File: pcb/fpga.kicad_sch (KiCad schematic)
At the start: 45 parts, among them U1 XC7A50T-FTG256, U2 410-251-B, U3 S70KL1283DPBHV020, U4 W25Q128JVS, Y1 ASE-20MHz

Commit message: layout prep
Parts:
- C1, C10, C11, C12, C13, C14, C15, C16, C17, C18, C19, C2, C20, C21, C22, C23, C24, C25, C26, C27, C28, C29, C3, C30, C4, C5, C6, C7, C8, C9: footprint (none) -> Capacitor_SMD:C_0805_2012Metric_Pad1.18x1.45mm_HandSolder
- R1, R10, R2, R3, R4, R5, R6, R7, R8, R9: footprint (none) -> Resistor_SMD:R_0805_2012Metric_Pad1.20x1.40mm_HandSolder
- U2: footprint IC11_410-251-B_DGT -> footprints:IC11_410-251-B_DGT
- U3: footprint (none) -> S70KL1283DPBHV020:BGA24C100P5X5_600X800X100
- Y1: footprint Oscillator:Oscillator_DIP-14 -> Oscillator:Oscillator_SMD_Abracon_ASV-4Pin_7.0x5.1mm_HandSoldering
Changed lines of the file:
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@@
 			)
 		)
-		(property "Footprint" ""
+		(property "Footprint" "Capacitor_SMD:C_0805_2012Metric_Pad1.18x1.45mm_HandSolder"
 			(at 360.3752 229.87 0)
 			(hide yes)
@@
 			)
 		)
-		(property "Footprint" ""
+		(property "Footprint" "Capacitor_SMD:C_0805_2012Metric_Pad1.18x1.45mm_HandSolder"
 			(at 276.5552 35.56 0)
 			(hide yes)
@@
 			)
 		)
-		(property "Footprint" ""
+		(property "Footprint" "Resistor_SMD:R_0805_2012Metric_Pad1.20x1.40mm_HandSolder"
 			(at 106.68 79.248 90)
 			(hide yes)
@@
 			)
 		)
-		(property "Footprint" ""
+		(property "Footprint" "Capacitor_SMD:C_0805_2012Metric_Pad1.18x1.45mm_HandSolder"
 			(at 261.3152 35.56 0)
 			(hide yes)
@@
 			)
 		)
-		(property "Footprint" ""
+		(property "Footprint" "Capacitor_SMD:C_0805_2012Metric_Pad1.18x1.45mm_HandSolder"
 			(at 284.1752 35.56 0)
 			(hide yes)
@@
 			)
 		)
-		(property "Footprint" ""
+		(property "Footprint" "Capacitor_SMD:C_0805_2012Metric_Pad1.18x1.45mm_HandSolder"
 			(at 307.0352 35.56 0)
 			(hide yes)
@@
 			)
 		)
-		(property "Footprint" ""
+		(property "Footprint" "Resistor_SMD:R_0805_2012Metric_Pad1.20x1.40mm_HandSolder"
 			(at 164.592 62.23 90)
 			(hide yes)
@@
 			)
 		)
-		(property "Footprint" ""
+		(property "Footprint" "Capacitor_SMD:C_0805_2012Metric_Pad1.18x1.45mm_HandSolder"
 			(at 268.9352 35.56 0)
 			(hide yes)
@@
 			)
 		)
-		(property "Footprint" ""
+		(property "Footprint" "Resistor_SMD:R_0805_2012Metric_Pad1.20x1.40mm_HandSolder"
 			(at 119.38 57.658 90)
 			(hide yes)
@@
 			)
 		)
-		(property "Footprint" ""
+		(property "Footprint" "Capacitor_SMD:C_0805_2012Metric_Pad1.18x1.45mm_HandSolder"
 			(at 164.7952 226.06 0)
 			(hide yes)
@@
 			)
 		)
-		(property "Footprint" ""
+		(property "Footprint" "Capacitor_SMD:C_0805_2012Metric_Pad1.18x1.45mm_HandSolder"
 			(at 176.2252 49.53 0)
 			(hide yes)
@@
 			)
 		)
-		(property "Footprint" ""
+		(property "Footprint" "Capacitor_SMD:C_0805_2012Metric_Pad1.18x1.45mm_HandSolder"
 			(at 296.8752 229.87 0)
 			(hide yes)
@@
 			)
 		)
-		(property "Footprint" ""
+		(property "Footprint" "Capacitor_SMD:C_0805_2012Metric_Pad1.18x1.45mm_HandSolder"
 			(at 157.1752 226.06 0)
 			(hide yes)
@@
 			)
 		)
-		(property "Footprint" ""
+		(property "Footprint" "Capacitor_SMD:C_0805_2012Metric_Pad1.18x1.45mm_HandSolder"
 			(at 289.2552 229.87 0)
 			(hide yes)
@@
 			)
 		)
-		(property "Footprint" ""
+		(property "Footprint" "Capacitor_SMD:C_0805_2012Metric_Pad1.18x1.45mm_HandSolder"
 			(at 352.7552 229.87 0)
 			(hide yes)
@@
 			)
 		)
-		(property "Footprint" ""
+		(property "Footprint" "Capacitor_SMD:C_0805_2012Metric_Pad1.18x1.45mm_HandSolder"
 			(at 354.0252 35.56 0)
 			(hide yes)
@@
 			)
 		)
-		(property "Footprint" ""
+		(property "Footprint" "Resistor_SMD:R_0805_2012Metric_Pad1.20x1.40mm_HandSolder"
 			(at 173.482 62.23 90)
 			(hide yes)
@@
 			)
 		)
-		(property "Footprint" ""
+		(property "Footprint" "Capacitor_SMD:C_0805_2012Metric_Pad1.18x1.45mm_HandSolder"
 			(at 312.1152 229.87 0)
 			(hide yes)
@@
 			)
 		)
-		(property "Footprint" ""
+		(property "Footprint" "Capacitor_SMD:C_0805_2012Metric_Pad1.18x1.45mm_HandSolder"
 			(at 346.4052 35.56 0)
 			(hide yes)
@@
 			)
 		)
-		(property "Footprint" ""
+		(property "Footprint" "Capacitor_SMD:C_0805_2012Metric_Pad1.18x1.45mm_HandSolder"
 			(at 314.6552 35.56 0)
 			(hide yes)
@@
 			)
 		)
-		(property "Footprint" ""
+		(property "Footprint" "Capacitor_SMD:C_0805_2012Metric_Pad1.18x1.45mm_HandSolder"
 			(at 383.2352 229.87 0)
 			(hide yes)
@@
 			)
 		)
-		(property "Footprint" ""
+		(property "Footprint" "Capacitor_SMD:C_0805_2012Metric_Pad1.18x1.45mm_HandSolder"
 			(at 345.1352 229.87 0)
 			(hide yes)
@@
 			)
 		)
-		(property "Footprint" ""
+		(property "Footprint" "Capacitor_SMD:C_0805_2012Metric_Pad1.18x1.45mm_HandSolder"
 			(at 230.1748 121.92 0)
 			(hide yes)
@@
 			)
 		)
-		(property "Footprint" ""
+		(property "Footprint" "Resistor_SMD:R_0805_2012Metric_Pad1.20x1.40mm_HandSolder"
 			(at 119.38 62.738 90)
 			(hide yes)
@@
 			)
 		)
-		(property "Footprint" ""
+		(property "Footprint" "Resistor_SMD:R_0805_2012Metric_Pad1.20x1.40mm_HandSolder"
 			(at 119.38 52.578 90)
 			(hide yes)
@@
 			)
 		)
-		(property "Footprint" ""
+		(property "Footprint" "Capacitor_SMD:C_0805_2012Metric_Pad1.18x1.45mm_HandSolder"
 			(at 367.9952 229.87 0)
 			(hide yes)
@@
 			)
 		)
-		(property "Footprint" ""
+		(property "Footprint" "Capacitor_SMD:C_0805_2012Metric_Pad1.18x1.45mm_HandSolder"
 			(at 323.5452 35.56 0)
 			(hide yes)
@@
 			)
 		)
-		(property "Footprint" ""
+		(property "Footprint" "Resistor_SMD:R_0805_2012Metric_Pad1.20x1.40mm_HandSolder"
 			(at 106.68 84.328 90)
 			(hide yes)
@@
 			)
 		)
-		(property "Footprint" ""
+		(property "Footprint" "Capacitor_SMD:C_0805_2012Metric_Pad1.18x1.45mm_HandSolder"
 			(at 299.4152 35.56 0)
 			(hide yes)
@@
 			)
 		)
-		(property "Footprint" ""
+		(property "Footprint" "Resistor_SMD:R_0805_2012Metric_Pad1.20x1.40mm_HandSolder"
 			(at 106.68 89.408 90)
 			(hide yes)
@@
 			)
 		)
-		(property "Footprint" ""
+		(property "Footprint" "Resistor_SMD:R_0805_2012Metric_Pad1.20x1.40mm_HandSolder"
 			(at 155.702 62.23 90)
 			(hide yes)
@@
 			)
 		)
-		(property "Footprint" ""
+		(property "Footprint" "Capacitor_SMD:C_0805_2012Metric_Pad1.18x1.45mm_HandSolder"
 			(at 291.7952 35.56 0)
 			(hide yes)
@@
 			)
 		)
-		(property "Footprint" ""
+		(property "Footprint" "Resistor_SMD:R_0805_2012Metric_Pad1.20x1.40mm_HandSolder"
 			(at 106.68 94.488 90)
 			(hide yes)
@@
 			)
 		)
-		(property "Footprint" ""
+		(property "Footprint" "Capacitor_SMD:C_0805_2012Metric_Pad1.18x1.45mm_HandSolder"
 			(at 304.4952 229.87 0)
 			(hide yes)
@@
 			)
 		)
-		(property "Footprint" ""
+		(property "Footprint" "Capacitor_SMD:C_0805_2012Metric_Pad1.18x1.45mm_HandSolder"
 			(at 280.67 226.06 0)
 			(hide yes)
@@
 			)
 		)
-		(property "Footprint" ""
+		(property "Footprint" "Capacitor_SMD:C_0805_2012Metric_Pad1.18x1.45mm_HandSolder"
 			(at 361.6452 35.56 0)
 			(hide yes)
@@
 			)
 		)
-		(property "Footprint" ""
+		(property "Footprint" "Capacitor_SMD:C_0805_2012Metric_Pad1.18x1.45mm_HandSolder"
 			(at 369.2652 35.56 0)
 			(hide yes)
@@
 			)
 		)
-		(property "Footprint" ""
+		(property "Footprint" "S70KL1283DPBHV020:BGA24C100P5X5_600X800X100"
 			(at 152.4 88.9 0)
 			(hide yes)
@@
 			)
 		)
-		(property "Footprint" ""
+		(property "Footprint" "Capacitor_SMD:C_0805_2012Metric_Pad1.18x1.45mm_HandSolder"
 			(at 331.1652 35.56 0)
 			(hide yes)
@@
 			)
 		)
-		(property "Footprint" ""
+		(property "Footprint" "Capacitor_SMD:C_0805_2012Metric_Pad1.18x1.45mm_HandSolder"
 			(at 375.6152 229.87 0)
 			(hide yes)
@@
 			)
 		)
-		(property "Footprint" ""
+		(property "Footprint" "Capacitor_SMD:C_0805_2012Metric_Pad1.18x1.45mm_HandSolder"
 			(at 338.7852 35.56 0)
 			(hide yes)
@@
 			)
 		)
-		(property "Footprint" "IC11_410-251-B_DGT"
+		(property "Footprint" "footprints:IC11_410-251-B_DGT"
 			(at 119.38 25.4 0)
 			(hide yes)
@@
 			)
 		)
-		(property "Footprint" "Oscillator:Oscillator_DIP-14"
+		(property "Footprint" "Oscillator:Oscillator_SMD_Abracon_ASV-4Pin_7.0x5.1mm_HandSoldering"
 			(at 259.08 124.46 0)
 			(hide yes)

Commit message: pcb/fpga: fix vga
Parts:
- added J?: DE15_Socket_HighDensity, Connector_Dsub:DSUB-15_Socket_EdgeMount_P2.77mm, symbol Connector:DE15_Socket_HighDensity
- added R? (x3): 510, symbol Device:R
- added R? (x3): 2.0k, symbol Device:R
- added R? (x3): 1.0k, symbol Device:R
- added R? (x2): 100, symbol Device:R
- added R? (x3): 3.9k, symbol Device:R
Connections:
- net +3V3: now also U1.M3 (VCCO_34), U1.R4 (VCCO_34), U1.T1 (VCCO_34)
- net GND: now also J?.10, J?.5, J?.6, J?.7, J?.8; no longer U1.M3 (VCCO_34), U1.R4 (VCCO_34), U1.T1 (VCCO_34)
- net at U1.M5 (IO_L6P_T0_34): now also R?.2
- net at U1.N1 (IO_L4P_T0_34): now also R?.2
- net at U1.N2 (IO_L3N_T0_DQS_34): now also R?.2
- net at U1.N4 (IO_L6N_T0_VREF_34): now also R?.2
- net at U1.P1 (IO_L4N_T0_34): now also R?.2
- net at U1.P3 (IO_L5N_T0_34): now also R?.2
- net at U1.P4 (IO_L5P_T0_34): now also R?.2
- net at U1.P5 (IO_L10P_T1_34): now also R?.2
- net at U1.R1 (IO_L7N_T1_34): now also R?.2
- net at U1.R2 (IO_L7P_T1_34): now also R?.2
- net at U1.R3 (IO_L8P_T1_34): now also R?.2
- net at U1.T2 (IO_L8N_T1_34): now also R?.2
- net at U1.T3 (IO_L9N_T1_DQS_34): now also R?.2
- net at U1.T4 (IO_L9P_T1_DQS_34): now also R?.2
- new net BLUE_ANALOG: J?.3, R?.1, R?.1, R?.1, R?.1
- new net GREEN_ANALOG: J?.2, R?.1, R?.1, R?.1, R?.1
- new net HSYNC: J?.13, R?.1
- new net RED_ANALOG: J?.1, R?.1, R?.1, R?.1, R?.1
- new net VSYNC: J?.14, R?.1
- no-connect marks 138 -> 129
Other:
- moved on the sheet: C1, C10, C12, C14, C16, C2, C21, C23, C25, C27, C29, C30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

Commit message: updates labels
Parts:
- gave numbers to parts that had none: 15
- renumbered C3 to C1, C17 to C10, C18 to C11, C1 to C12, C19 to C13, C2 to C14, C20 to C15, C22 to C16, C24 to C17, C21 to C18, C8 to C19, C4 to C2, C26 to C20, C23 to C21, C10 to C22, C28 to C23, C25 to C24, C12 to C25, C27 to C26, C14 to C27, C29 to C28, C16 to C29, C5 to C3, C6 to C4, C7 to C5, C9 to C6, C11 to C7, C13 to C8, C15 to C9, R8 to R22, R9 to R23, R10 to R24

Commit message: started layout
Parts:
- R10, R11, R12, R13, R14, R15, R16, R17, R18, R19, R20, R21, R8, R9: footprint (none) -> Resistor_SMD:R_0805_2012Metric_Pad1.20x1.40mm_HandSolder
- U2: footprint footprints:IC11_410-251-B_DGT -> 410_251_B:IC11_410-251-B_DGT
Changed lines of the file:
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@@
 			)
 		)
-		(property "Footprint" ""
+		(property "Footprint" "Resistor_SMD:R_0805_2012Metric_Pad1.20x1.40mm_HandSolder"
 			(at 129.54 221.742 90)
 			(hide yes)
@@
 			)
 		)
-		(property "Footprint" ""
+		(property "Footprint" "Resistor_SMD:R_0805_2012Metric_Pad1.20x1.40mm_HandSolder"
 			(at 129.54 216.662 90)
 			(hide yes)
@@
 			)
 		)
-		(property "Footprint" ""
+		(property "Footprint" "Resistor_SMD:R_0805_2012Metric_Pad1.20x1.40mm_HandSolder"
 			(at 129.54 211.582 90)
 			(hide yes)
@@
 			)
 		)
-		(property "Footprint" ""
+		(property "Footprint" "Resistor_SMD:R_0805_2012Metric_Pad1.20x1.40mm_HandSolder"
 			(at 129.54 219.202 90)
 			(hide yes)
@@
 			)
 		)
-		(property "Footprint" ""
+		(property "Footprint" "Resistor_SMD:R_0805_2012Metric_Pad1.20x1.40mm_HandSolder"
 			(at 129.54 234.442 90)
 			(hide yes)
@@
 			)
 		)
-		(property "Footprint" ""
+		(property "Footprint" "Resistor_SMD:R_0805_2012Metric_Pad1.20x1.40mm_HandSolder"
 			(at 129.54 214.122 90)
 			(hide yes)
@@
 			)
 		)
-		(property "Footprint" ""
+		(property "Footprint" "Resistor_SMD:R_0805_2012Metric_Pad1.20x1.40mm_HandSolder"
 			(at 129.54 224.282 90)
 			(hide yes)
@@
 			)
 		)
-		(property "Footprint" ""
+		(property "Footprint" "Resistor_SMD:R_0805_2012Metric_Pad1.20x1.40mm_HandSolder"
 			(at 129.54 226.822 90)
 			(hide yes)
@@
 			)
 		)
-		(property "Footprint" ""
+		(property "Footprint" "Resistor_SMD:R_0805_2012Metric_Pad1.20x1.40mm_HandSolder"
 			(at 129.54 231.902 90)
 			(hide yes)
@@
 			)
 		)
-		(property "Footprint" ""
+		(property "Footprint" "Resistor_SMD:R_0805_2012Metric_Pad1.20x1.40mm_HandSolder"
 			(at 129.54 229.362 90)
 			(hide yes)
@@
 			)
 		)
-		(property "Footprint" ""
+		(property "Footprint" "Resistor_SMD:R_0805_2012Metric_Pad1.20x1.40mm_HandSolder"
 			(at 129.54 203.962 90)
 			(hide yes)
@@
 			)
 		)
-		(property "Footprint" ""
+		(property "Footprint" "Resistor_SMD:R_0805_2012Metric_Pad1.20x1.40mm_HandSolder"
 			(at 129.54 206.502 90)
 			(hide yes)
@@
 			)
 		)
-		(property "Footprint" ""
+		(property "Footprint" "Resistor_SMD:R_0805_2012Metric_Pad1.20x1.40mm_HandSolder"
 			(at 129.54 236.982 90)
 			(hide yes)
@@
 			)
 		)
-		(property "Footprint" "footprints:IC11_410-251-B_DGT"
+		(property "Footprint" "410_251_B:IC11_410-251-B_DGT"
 			(at 119.38 25.4 0)
 			(hide yes)
@@
 			)
 		)
-		(property "Footprint" ""
+		(property "Footprint" "Resistor_SMD:R_0805_2012Metric_Pad1.20x1.40mm_HandSolder"
 			(at 129.54 209.042 90)
 			(hide yes)

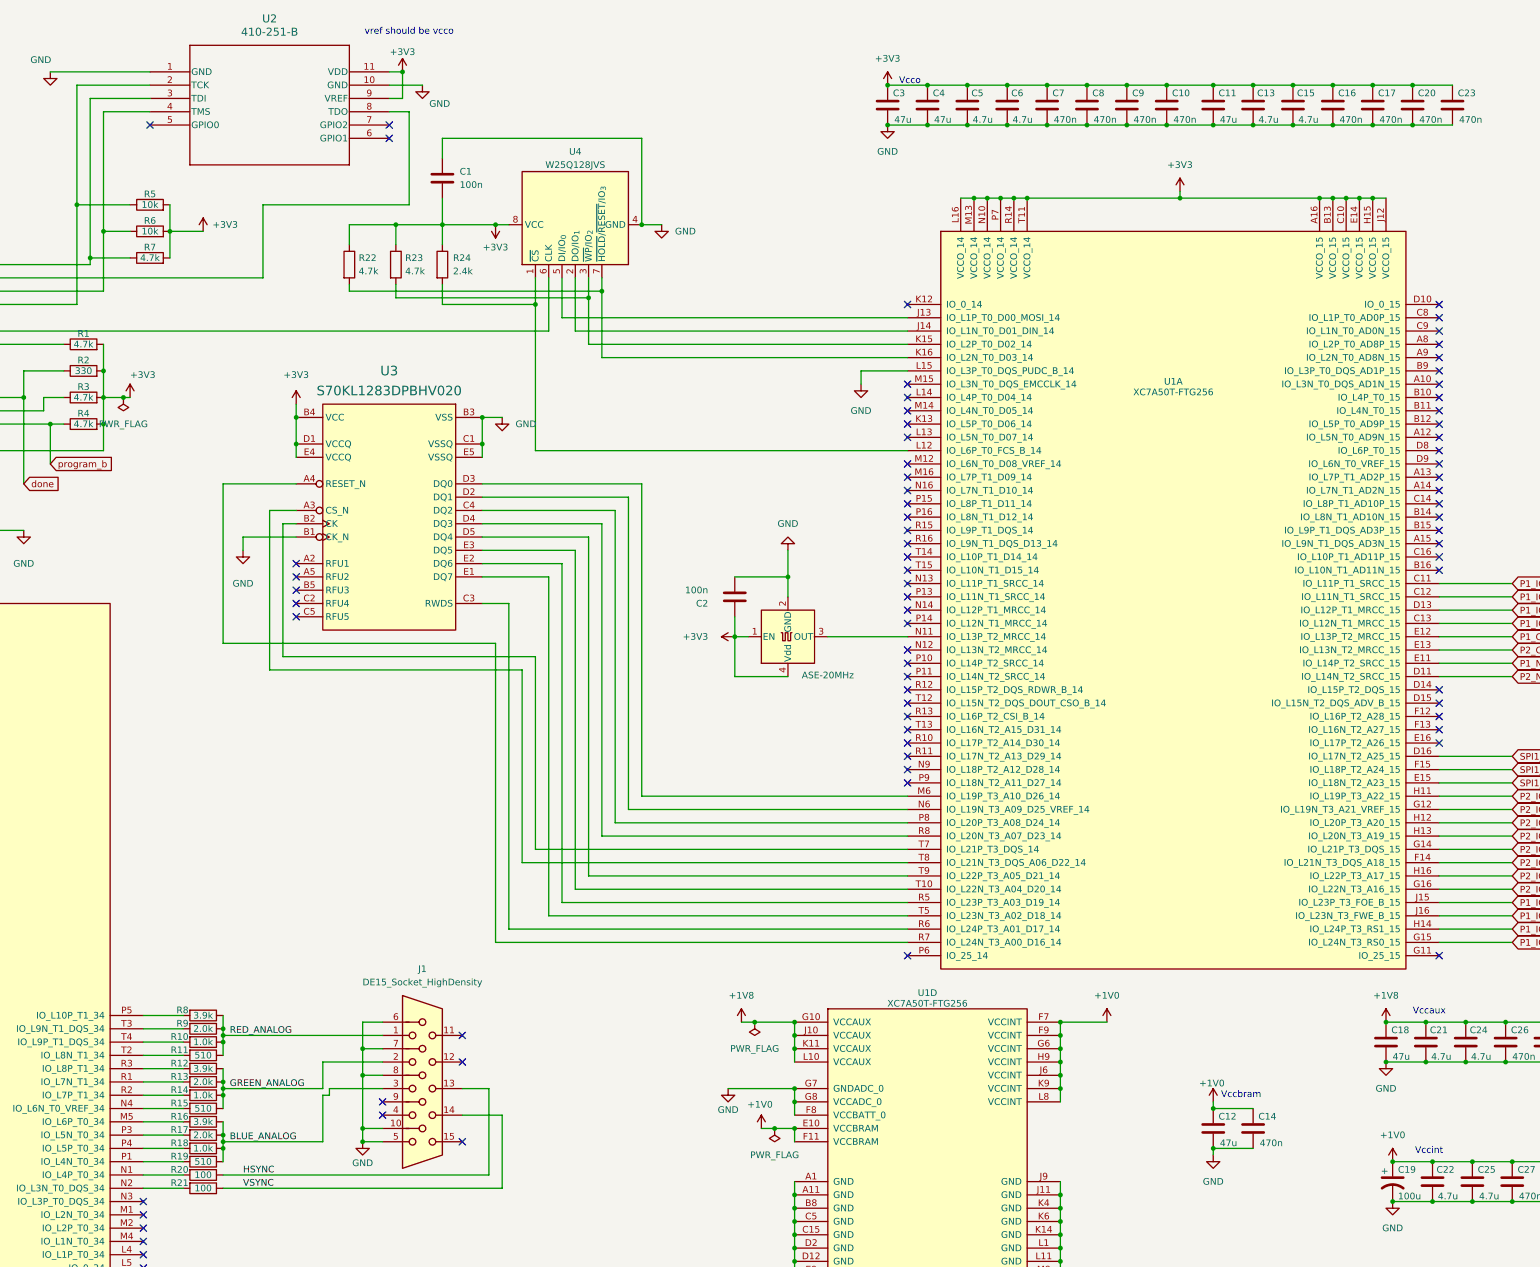
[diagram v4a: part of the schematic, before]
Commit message: pcb: finalize erc
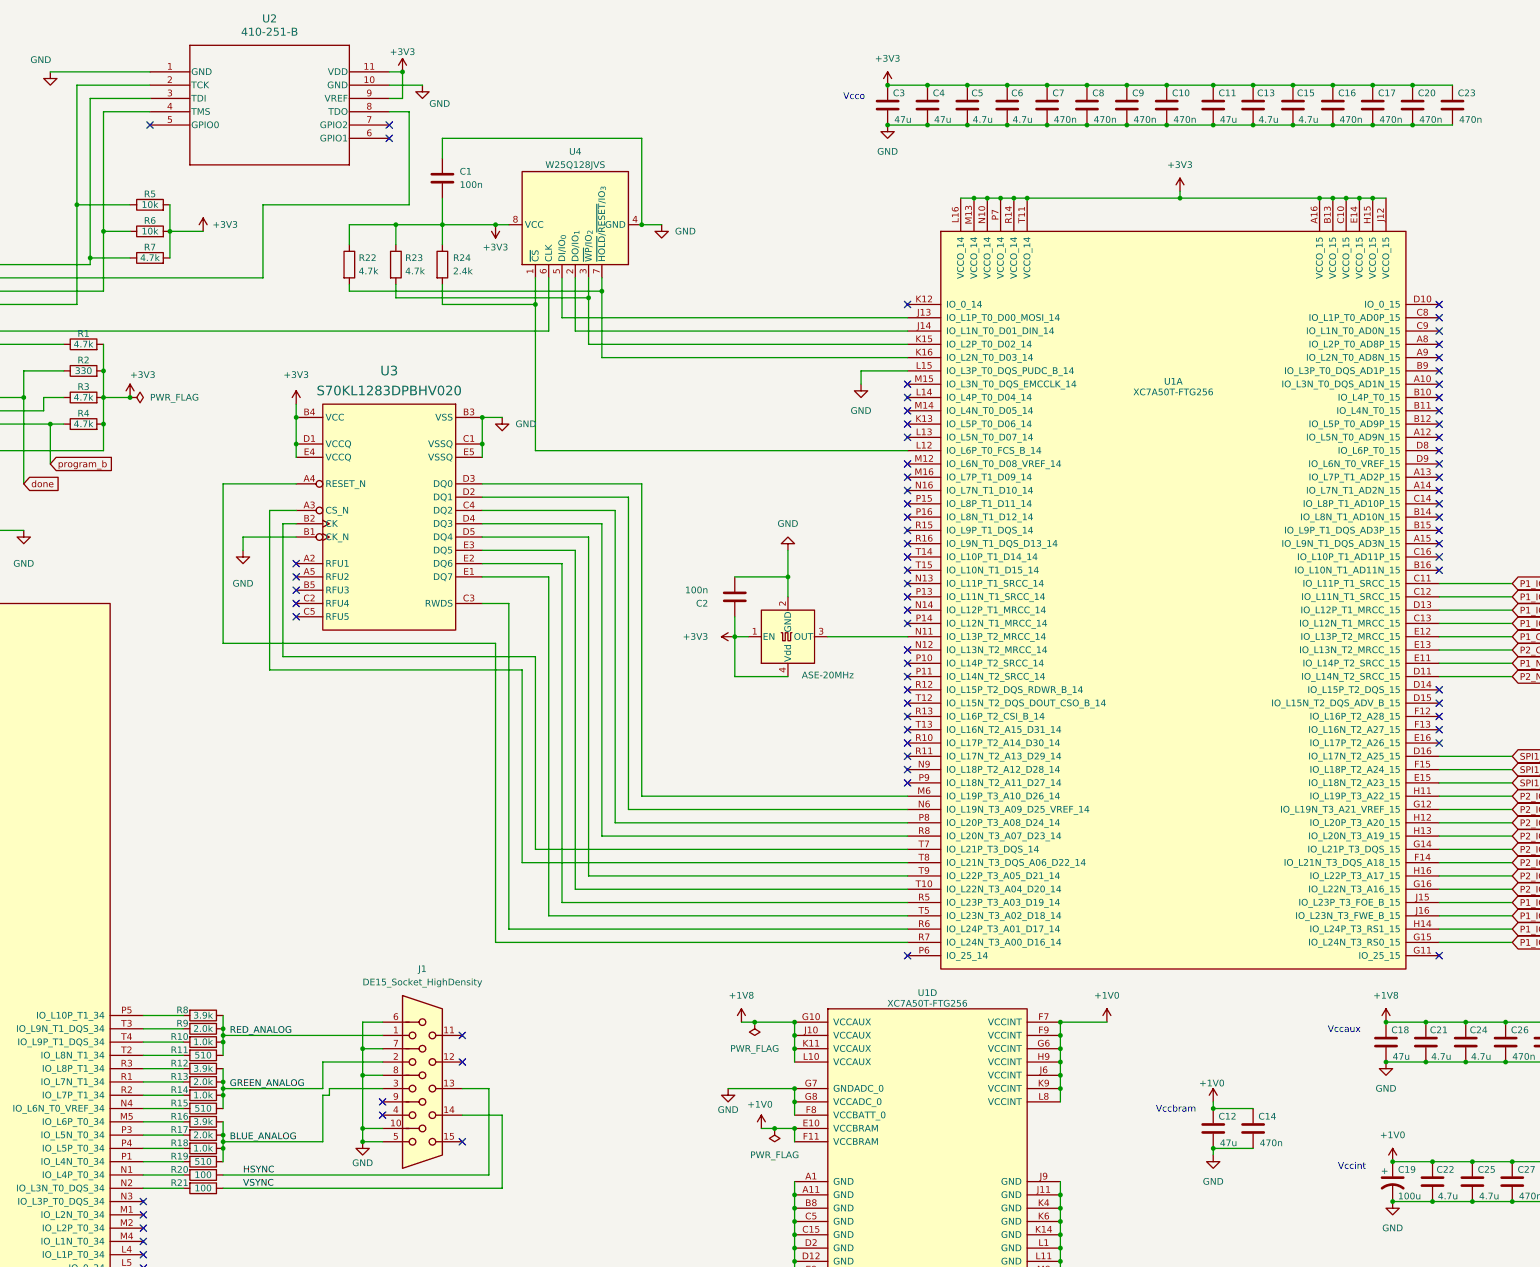
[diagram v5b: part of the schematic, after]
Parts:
- U3: symbol S70KL1283DPBHV020:S70KL1283DPBHV020 -> S70KL1283DPBHV02:S70KL1283DPBHV020
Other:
- note removed: "vref should be vcco"
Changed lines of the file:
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@@
 	(generator_version "10.0")
 	(paper "A3")
-	(text "vref should be vcco"
-		(exclude_from_sim no)
-		(at 168.91 17.78 0)
-		(effects
-			(font
-				(size 1.27 1.27)
-			)
-		)
-	)
 	(text "Vccbram\n"
 		(exclude_from_sim no)
-		(at 327.914 220.98 0)
+		(at 315.468 223.774 0)
 		(effects
 			(font
@@
 	(text "Vccaux"
 		(exclude_from_sim no)
-		(at 367.03 205.74 0)
+		(at 350.774 209.296 0)
 		(effects
 			(font
@@
 	(text "Vccint"
 		(exclude_from_sim no)
-		(at 366.522 232.41 0)
+		(at 351.79 235.458 0)
 		(effects
 			(font
@@
 	(text "Vcco"
 		(exclude_from_sim no)
-		(at 266.7 27.94 0)
+		(at 256.032 30.988 0)
 		(effects
 			(font
@@
 	)
 	(junction
+		(at 115.57 87.63)
+		(diameter 0)
+		(color 0 0 0 0)
+	)
+	(junction
 		(at 322.58 223.52)
 		(diameter 0)
@@
 	)
 	(junction
-		(at 114.3 87.63)
-		(diameter 0)
-		(color 0 0 0 0)
-	)
-	(junction
 		(at 242.57 245.11)
 		(diameter 0)
@@
 	(wire
 		(pts
-			(xy 114.3 87.63) (xy 115.57 87.63)
-		)
-		(stroke
-			(width 0)
-			(type default)
-		)
-	)
-	(wire
-		(pts
 			(xy 105.41 27.94) (xy 105.41 50.8)
 		)
@@
 	(wire
 		(pts
-			(xy 110.49 87.63) (xy 114.3 87.63)
+			(xy 110.49 87.63) (xy 115.57 87.63)
 		)
 		(stroke
@@
 	)
 	(symbol
-		(lib_id "S70KL1283DPBHV020:S70KL1283DPBHV020")
+		(lib_id "S70KL1283DPBHV02:S70KL1283DPBHV020")
 		(at 152.4 88.9 0)
 		(unit 1)
@@
 	(symbol
 		(lib_id "power:PWR_FLAG")
-		(at 114.3 87.63 180)
+		(at 115.57 87.63 270)
 		(unit 1)
 		(body_style 1)
@@
 		(fields_autoplaced yes)
 		(property "Reference" "#FLG01"
-			(at 114.3 89.535 0)
+			(at 117.475 87.63 0)
 			(hide yes)
 			(show_name no)
@@
 		)
 		(property "Value" "PWR_FLAG"
-			(at 114.3 92.71 0)
+			(at 119.38 87.6299 90)
 			(show_name no)
 			(do_not_autoplace no)
@@
 					(size 1.27 1.27)
 				)
+				(justify left)
 			)
 		)
 		(property "Footprint" ""
-			(at 114.3 87.63 0)
+			(at 115.57 87.63 0)
 			(hide yes)
 			(show_name no)
@@
 		)
 		(property "Datasheet" ""
-			(at 114.3 87.63 0)
+			(at 115.57 87.63 0)
 			(hide yes)
 			(show_name no)
@@
 		)
 		(property "Description" "Special symbol for telling ERC where power comes from"
-			(at 114.3 87.63 0)
+			(at 115.57 87.63 0)
 			(hide yes)
 			(show_name no)
